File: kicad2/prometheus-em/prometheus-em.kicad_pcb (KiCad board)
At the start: 2 copper layers, 42 x 40 mm, 90 parts, among them IC1 RP2040, IC10 NJM2878F3-33-TE2, IC2 SIT2001BI-S2-33E-12.000000G, IC3 W25Q128JVSIQ, IC4 TB67H450FNG,EL, IC5 TB67H450FNG,EL, IC6 PCA9306DCUR, IC7 S-89431ACMC-HBVT2U, IC8 NJM2884U1-33-TE1, IC9 NJM12888F33-TE1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

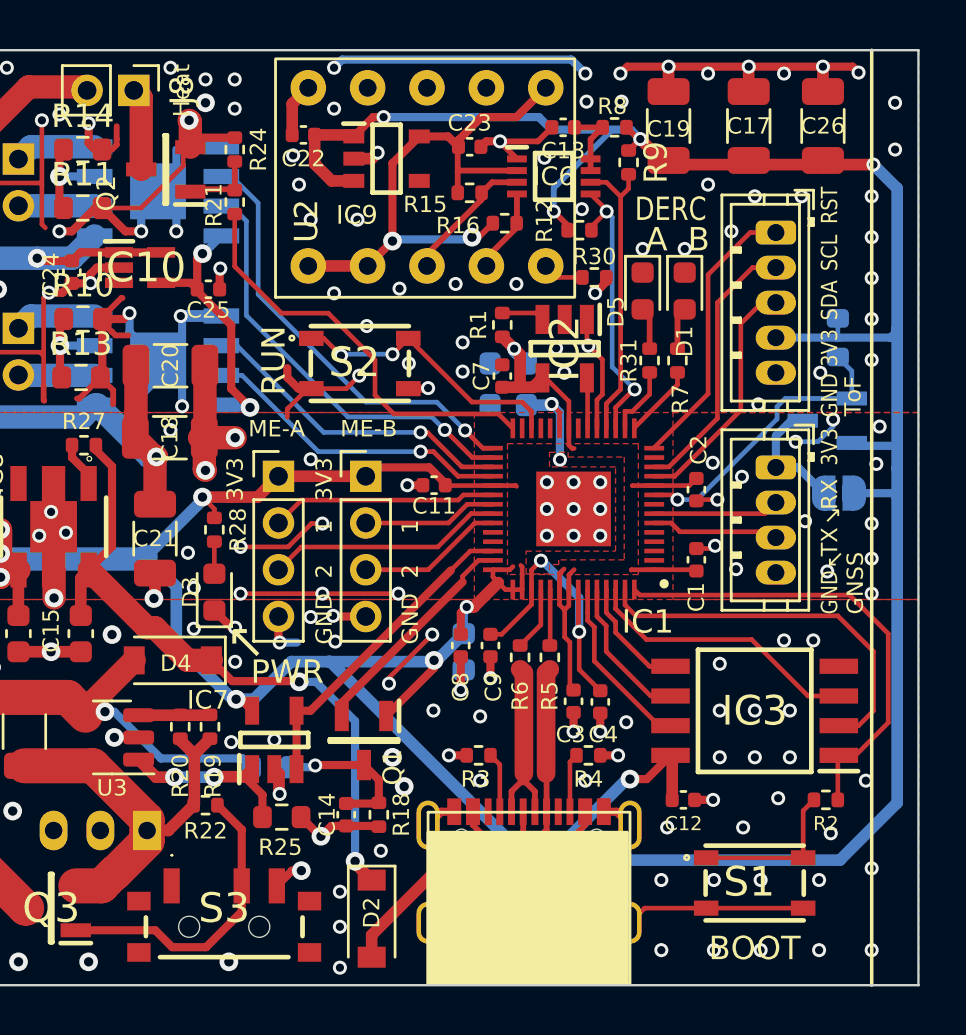
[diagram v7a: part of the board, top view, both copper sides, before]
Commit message: add eeprom for log
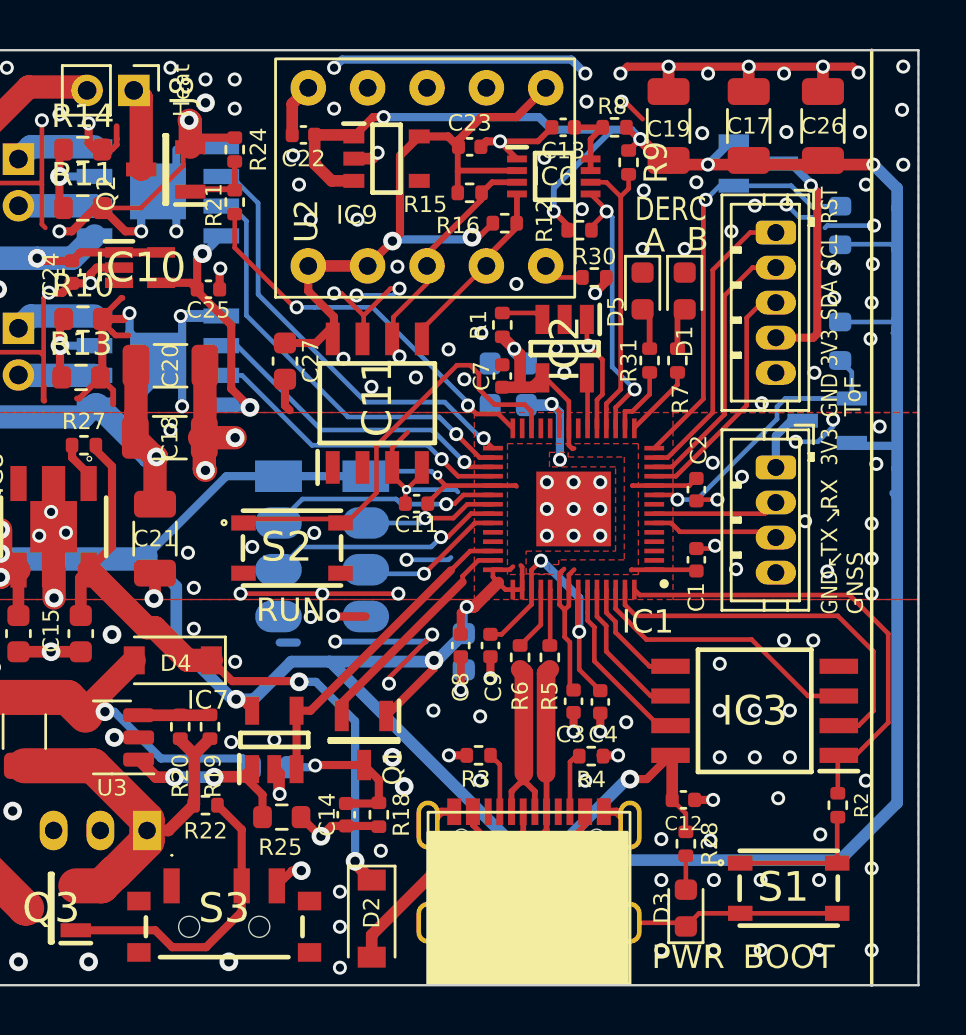
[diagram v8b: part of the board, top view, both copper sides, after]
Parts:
- removed JP1: GNSS_Power_Jumper, Jumper:SolderJumper-2_P1.3mm_Open_RoundedPad1.0x1.5mm
- added C27: 100n, Capacitor_SMD:C_0603_1608Metric, F.Cu at (50.9, 49.3)
- added IC11: S-24CM01CI-J8T1U4, SamacSys_Parts:SOT127P600X175-8N, F.Cu at (54.9, 51.1)
- added Q5: IRLML6402, SamacSys_Parts:SOT95P237X112-3N, B.Cu at (71.2, 40.9)
- added R26: 30k, Resistor_SMD:R_0603_1608Metric, B.Cu at (74.7, 43.5)
- J1, J3: footprint Connector_PinHeader_2.00mm:PinHeader_1x04_P2.00mm_Vertical -> tanekonsat:PinHeader_1x04_P2.00mm_Vertical; moved to B.Cu
- moved D3 24.3 mm to (68.0, 72.7)
- moved R28 24.2 mm to (68.0, 70.0)
- moved S2 8.41 mm to (51.2, 57.3)
- moved S1 1.47 mm to (72.5, 71.8)
- moved C11 1.09 mm to (56.5, 55.4)
- moved R2 0.56 mm to (74.5, 68.3), turned to 90 degrees
- moved R23 0.18 mm to (74.7, 48.5)
- moved R4 0.12 mm to (64.0, 66.2)
- turned J1 to 180 degrees
- turned J3 to 180 degrees
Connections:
- net /GPIO7_GNSS_RST renamed /GPIO7_GNSS_VCC
- IC1 pad 13: unconnected-(IC1-Pad13) -> /GPIO10_ToF_LPn
- IC1 pad 14: /GPIO14_ToF_RST -> /GPIO14_ToF_VCC
- J4 pad 1: /GPIO14_ToF_RST -> /GPIO10_ToF_LPn
- J4 pad 4: +3V3 -> Net-(J4-Pad4)
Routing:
- net /GPIO14_ToF_VCC: track 0.00 -> 17.9 mm, vias 0 -> 1
- net GND: track 171.0 -> 184.6 mm, vias 191 -> 198
- net /GPIO10_ToF_LPn: track 0.00 -> 12.8 mm
- net /GPIO14_ToF_RST: track 12.0 -> 0.00 mm
- net Net-(J4-Pad4): track 0.00 -> 9.94 mm, vias 0 -> 1
- net /RUN: track 12.1 -> 18.4 mm, vias 2 -> 0
- net +1V8: track 24.9 -> 30.3 mm
- net /IMU_SDA: track 3.93 -> 7.69 mm
- net /IMU_SCL: track 5.80 -> 8.92 mm
- net Net-(J2-Pad1): track 5.27 -> 2.77 mm
- net /GPIO17_Nichrome: track 17.9 -> 16.6 mm, vias 0 -> 2
- net Net-(R2-Pad1): track 6.82 -> 6.13 mm
- net +3V3: track 196.7 -> 197.3 mm, vias 13 -> 14
- net /GPIO22_MOE_A1: track 9.67 -> 9.85 mm, vias 0 -> 1
- net /GPIO25_MOE_B2: track 6.27 -> 6.41 mm, vias 0 -> 1
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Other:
- board text removed: "←"
